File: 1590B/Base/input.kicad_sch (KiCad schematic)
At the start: 17 parts, among them J201 Conn_02x04_Odd_Even, Q103 BC846, Q201 LS844, SW101 SW_Push_SPDT, U101 Daisy Seed

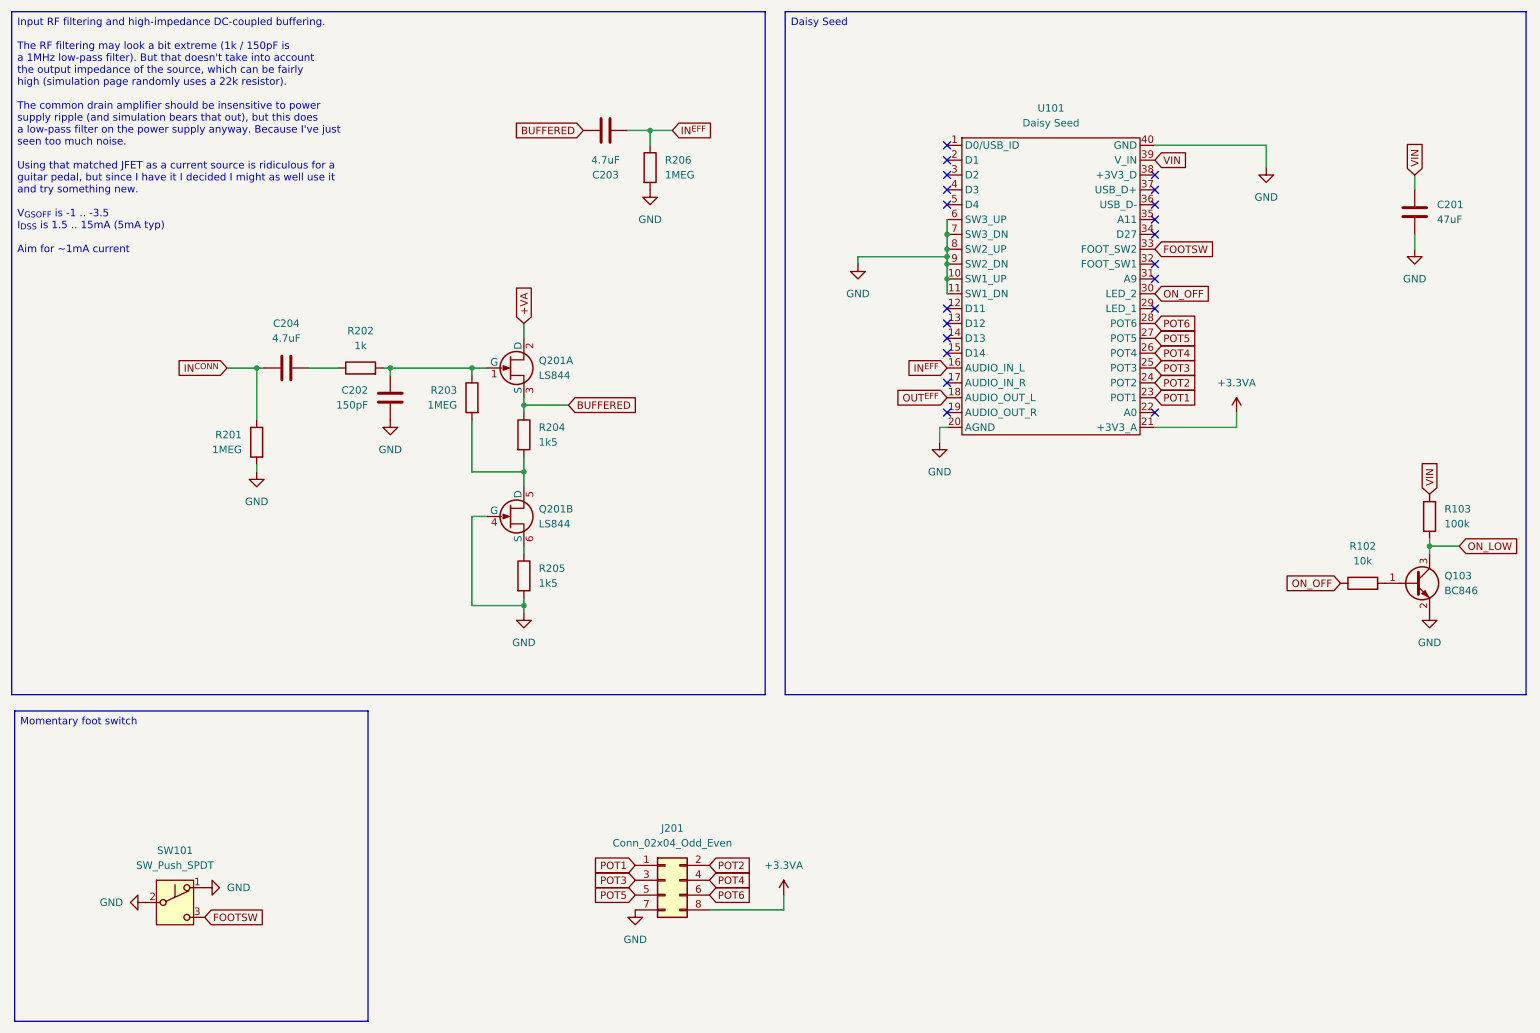
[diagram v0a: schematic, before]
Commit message: Update 1590B board for sanity
I had entirely forgotten the activity LED, which was really annoying
when testing.

Also, while the transistor follower / capacitor multiplier on the analog
power supply was interesting for some low frequency power supply ripple
removal in simulation, it doesn't actually make any sense with any
modern power supply, so just do a regular RC filter for high
frequencies, which is what actually matters.

Together with the fixed potentiometer board, I think this should now
work nicely.

Famous last words.

Signed-off-by: Linus Torvalds <torvalds@linux-foundation.org>
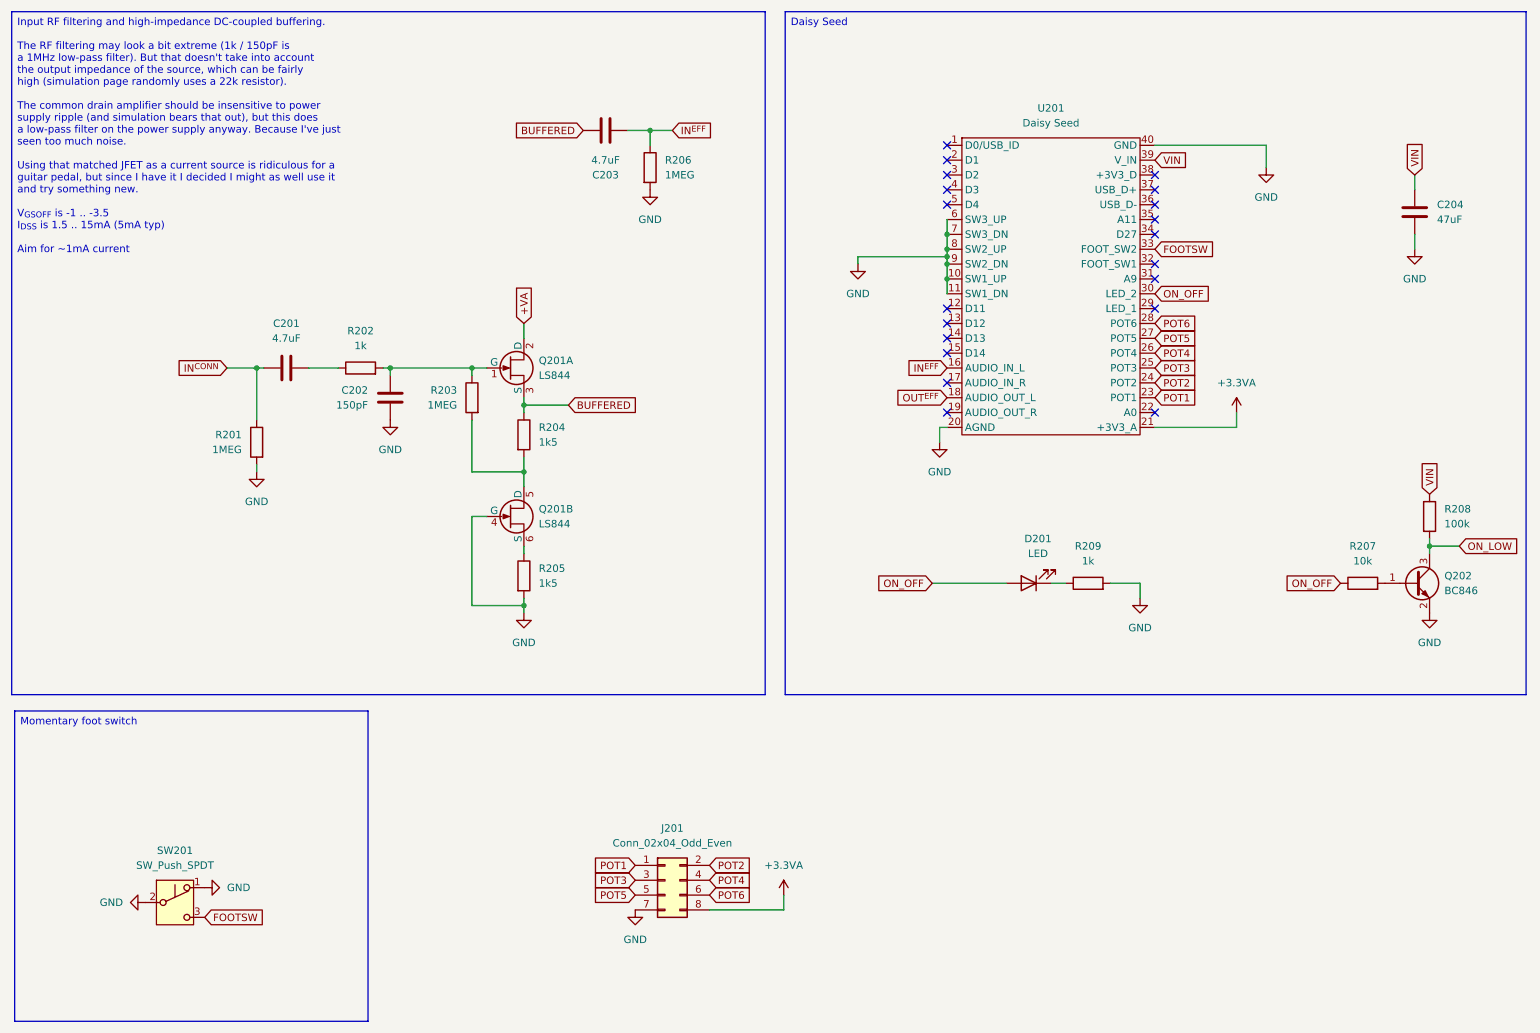
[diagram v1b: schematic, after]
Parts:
- added D201: LED, LED_THT:LED_D5.0mm, symbol Device:LED
- added R209: 1k, Resistor_SMD:R_0805_2012Metric, symbol Device:R
- renumbered C204 to C201, C201 to C204, Q103 to Q202, R102 to R207, R103 to R208, SW101 to SW201, U101 to U201
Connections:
- net GND: now also R209.2
- net ON_OFF: now also D201.2 (A)
- new net: D201.1 (K), R209.1
